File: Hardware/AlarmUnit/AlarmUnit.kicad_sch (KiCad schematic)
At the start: 16 parts, among them J1 Screw_Terminal_01x08, J2 Screw_Terminal_01x08, J3 Screw_Terminal_01x08, U1 ESP32-POE-ISO, U2 PC817, U3 PC817, U4 PC817, U5 PC817, U6 PC817, U7 PC817

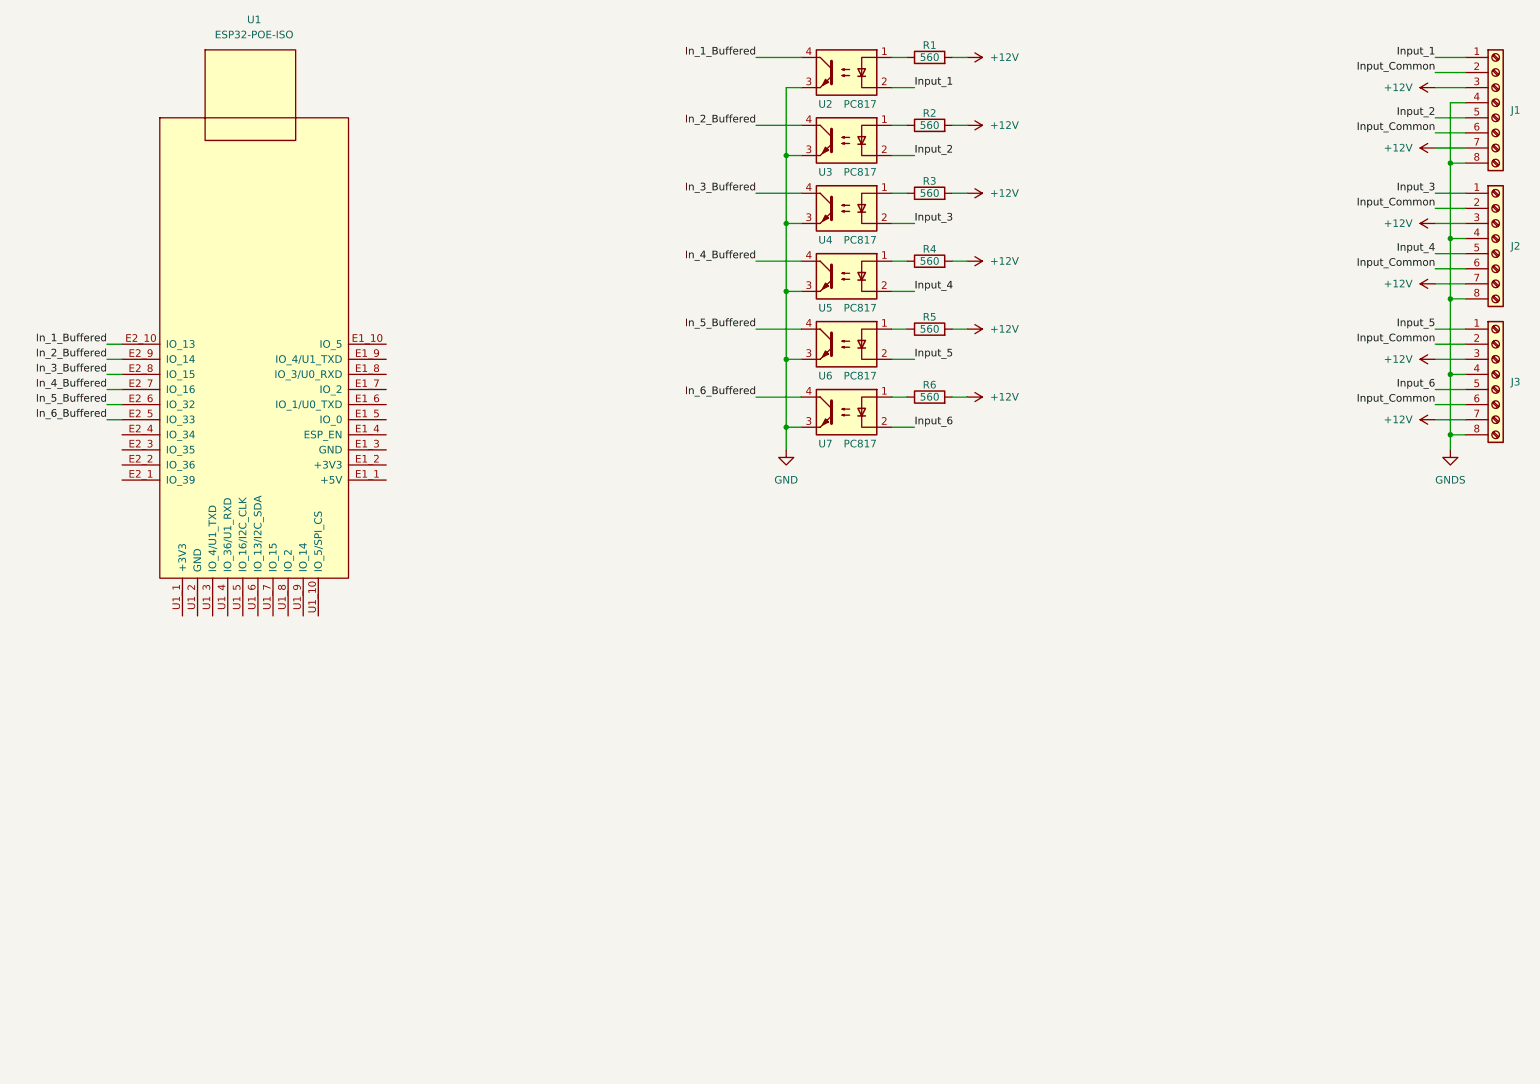
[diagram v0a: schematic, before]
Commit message: Working on hardware design to add outputs
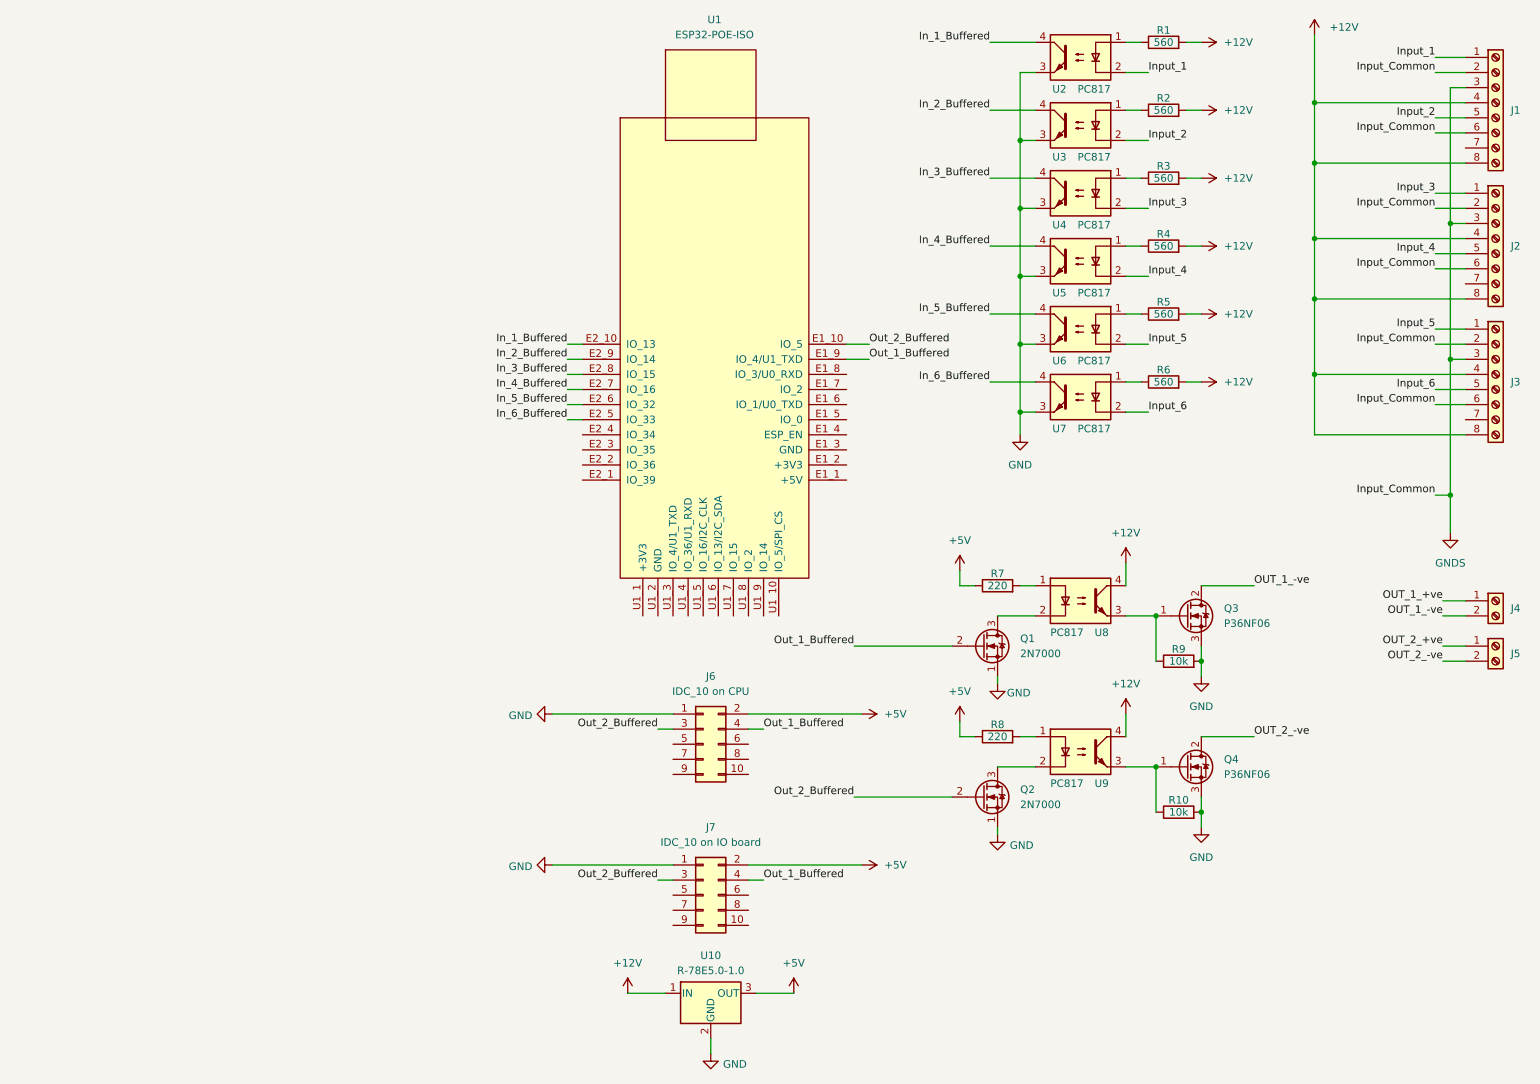
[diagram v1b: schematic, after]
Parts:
- added J4, J5: Screw_Terminal_01x02, symbol Connector:Screw_Terminal_01x02
- added J6: IDC_10 on CPU, symbol Connector_Generic:Conn_02x05_Odd_Even
- added J7: IDC_10 on IO board, symbol Connector_Generic:Conn_02x05_Odd_Even
- added Q1, Q2: 2N7000, Package_TO_SOT_THT:TO-92_Inline, symbol Transistor_FET:2N7000
- added Q3, Q4: P36NF06, Package_TO_SOT_THT:TO-220-3_Vertical, symbol Device:Q_NMOS_GDS
- added R10, R9: 10k, symbol Device:R
- added R7, R8: 220, symbol Device:R
- added U10: R-78E5.0-1.0, Converter_DCDC:Converter_DCDC_RECOM_R-78E-0.5_THT, symbol Regulator_Switching:R-78E5.0-1.0
- added U8, U9: PC817, Package_DIP:DIP-4_W7.62mm, symbol Isolator:PC817
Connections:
- net Input_Common is gone; now on net GNDS: J1.2 (Pin_2), J1.6 (Pin_6), J2.2 (Pin_2), J2.6 (Pin_6), J3.2 (Pin_2), J3.6 (Pin_6)
- net +12V: now also J1.4 (Pin_4), J1.8 (Pin_8), J2.4 (Pin_4), J2.8 (Pin_8), J3.4 (Pin_4), J3.8 (Pin_8), U10.1 (IN), U8.4, U9.4; no longer J1.3 (Pin_3), J1.7 (Pin_7), J2.3 (Pin_3), J2.7 (Pin_7), J3.3 (Pin_3), J3.7 (Pin_7)
- net GND: now also J6.1 (Pin_1), J7.1 (Pin_1), Q1.1 (S), Q2.1 (S), Q3.3 (S), Q4.3 (S), R10.2, R9.2, U10.2 (GND)
- net GNDS: now also J1.3 (Pin_3), J2.3 (Pin_3), J3.3 (Pin_3); no longer J1.4 (Pin_4), J1.8 (Pin_8), J2.4 (Pin_4), J2.8 (Pin_8), J3.4 (Pin_4), J3.8 (Pin_8)
- net Out_2_Buffered: now reaches U1.E1_10 (IO_5)
- net Out_2_Buffered: now also J6.3 (Pin_3), J7.3 (Pin_3), Q2.2 (G)
- net Out_1_Buffered: now reaches U1.E1_9 (IO_4/U1_TXD)
- net Out_1_Buffered: now also J6.4 (Pin_4), J7.4 (Pin_4), Q1.2 (G)
- new net: Q2.3 (D), U9.2
- new net: Q3.1 (G), R9.1, U8.3
- new net: Q4.1 (G), R10.1, U9.3
- new net: R7.2, U8.1
- new net: Q1.3 (D), U8.2
- new net: R8.2, U9.1
- new net +5V: J6.2 (Pin_2), J7.2 (Pin_2), R7.1, R8.1, U10.3 (OUT)
- new net OUT_1_+ve: J4.1 (Pin_1)
- new net OUT_1_-ve: J4.2 (Pin_2), Q3.2 (D)
- new net OUT_2_+ve: J5.1 (Pin_1)
- new net OUT_2_-ve: J5.2 (Pin_2), Q4.2 (D)
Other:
- moved on the sheet: R1, R2, R3, R4, R5, R6, U1, U2, U3, U4, U5, U6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

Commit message: Updated power circuits on alarm schematic
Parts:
- added D1: W02G, Diode_THT:Diode_Bridge_Round_D9.8mm, symbol Diode_Bridge:W02G
- added U11, U14: Lead-Acid-Charger, Converter_DCDC:Converter_DCDC_Murata_CRE1xxxxxxSC_THT, symbol Regulator_Switching:CRE1S2405SC
- added U12, U13: VRB1212YMD-5WR3, Converter_DCDC:Converter_DCDC_TRACO_TBA2-xxxx_Single_THT, symbol Converter_DCDC:TBA2-1212
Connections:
- net +12V: no longer U10.1 (IN)
- net GND: now also D1.3 (-), U11.1 (-VIN), U11.3 (-VOUT), U12.2 (-Vin), U13.2 (-Vin), U14.1 (-VIN), U14.3 (-VOUT)
- new net: D1.1 (+), U14.2 (+VIN)
- new net +12Va: U12.6 (+Vout)
- new net +12Vb: U13.6 (+Vout)
- new net +13.5V: U10.1 (IN), U11.2 (+VIN), U11.4 (+VOUT), U12.1 (+Vin), U13.1 (+Vin), U14.4 (+VOUT)
- new net 16V AC1: D1.4
- new net 16V AC2: D1.2
- new net GND_ISO: U12.4 (-Vout), U13.4 (-Vout)

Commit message: Schematic Update
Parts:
- removed U11: Lead-Acid-Charger, Converter_DCDC:Converter_DCDC_Murata_CRE1xxxxxxSC_THT, symbol Regulator_Switching:CRE1S2405SC
- removed U13: VRB1212YMD-5WR3, Converter_DCDC:Converter_DCDC_TRACO_TBA2-xxxx_Single_THT, symbol Converter_DCDC:TBA2-1212
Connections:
- net +12Va is gone; now on net +12V: U12.6 (+Vout)
- net +12V: now also U10.1 (IN)
- net +13.5V: no longer U10.1 (IN)
